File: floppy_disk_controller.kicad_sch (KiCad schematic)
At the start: 60 parts, among them J1 Conn_02x18_Odd_Even, U15 L78L05_TO92

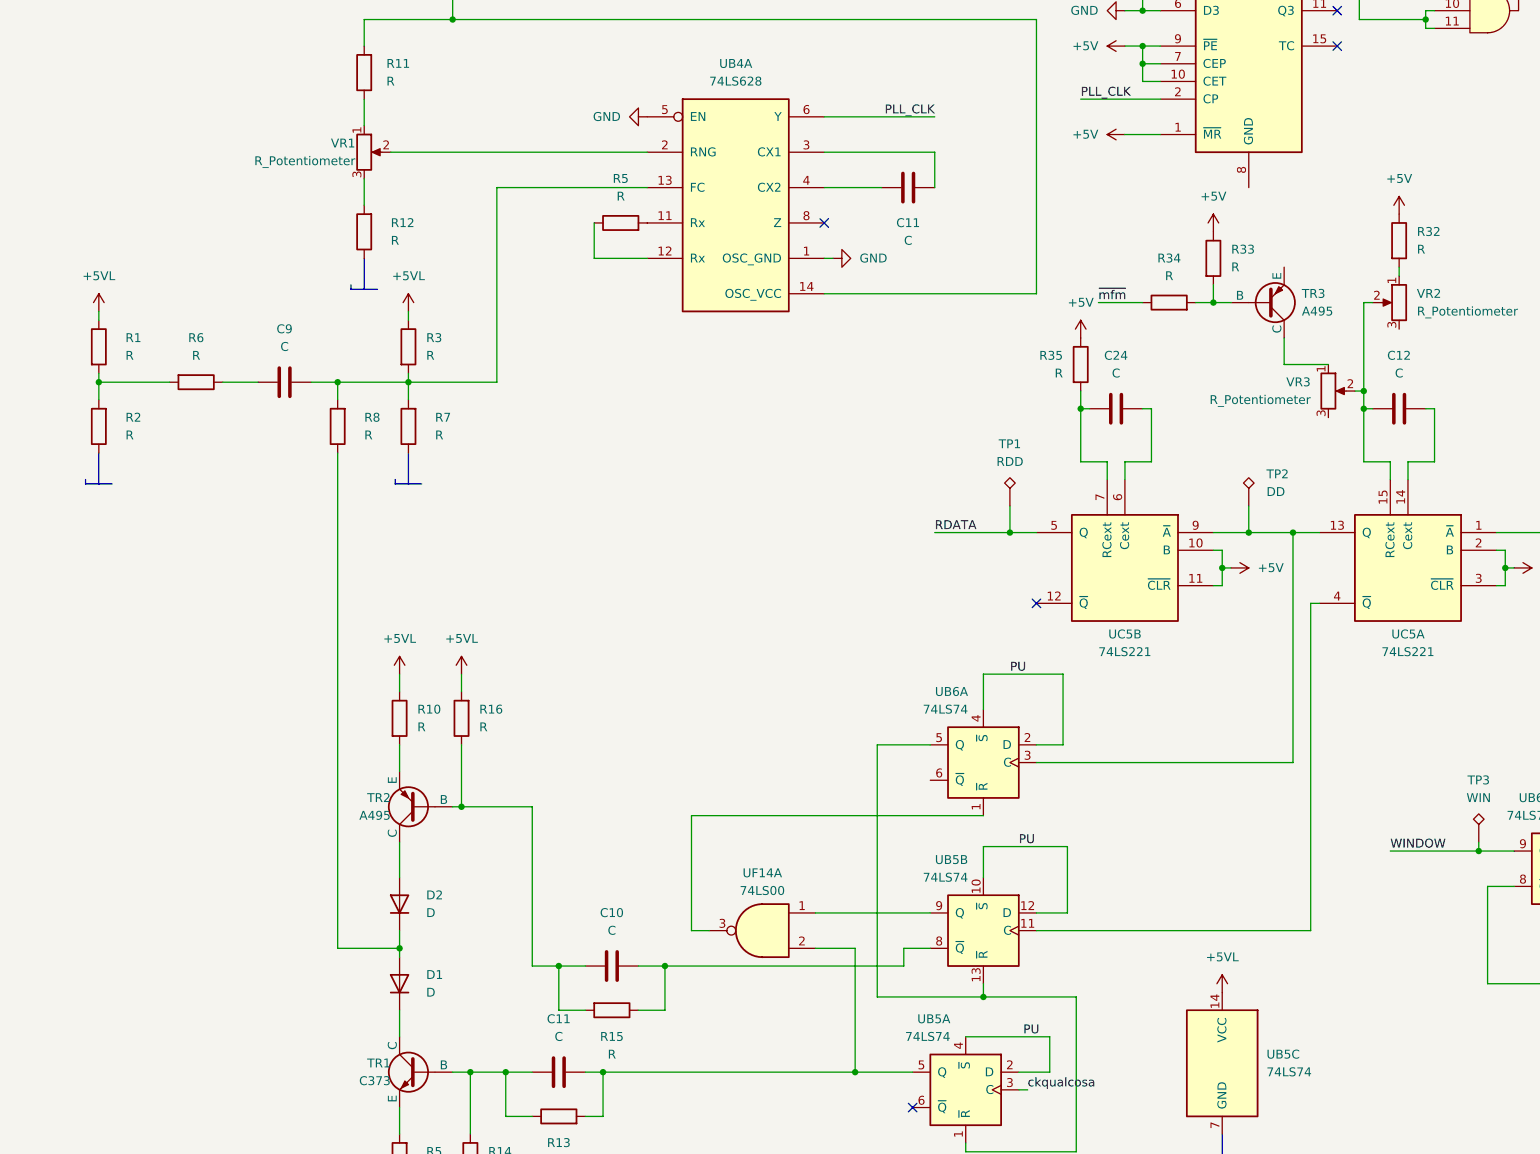
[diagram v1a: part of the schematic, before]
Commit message: Annotated all components
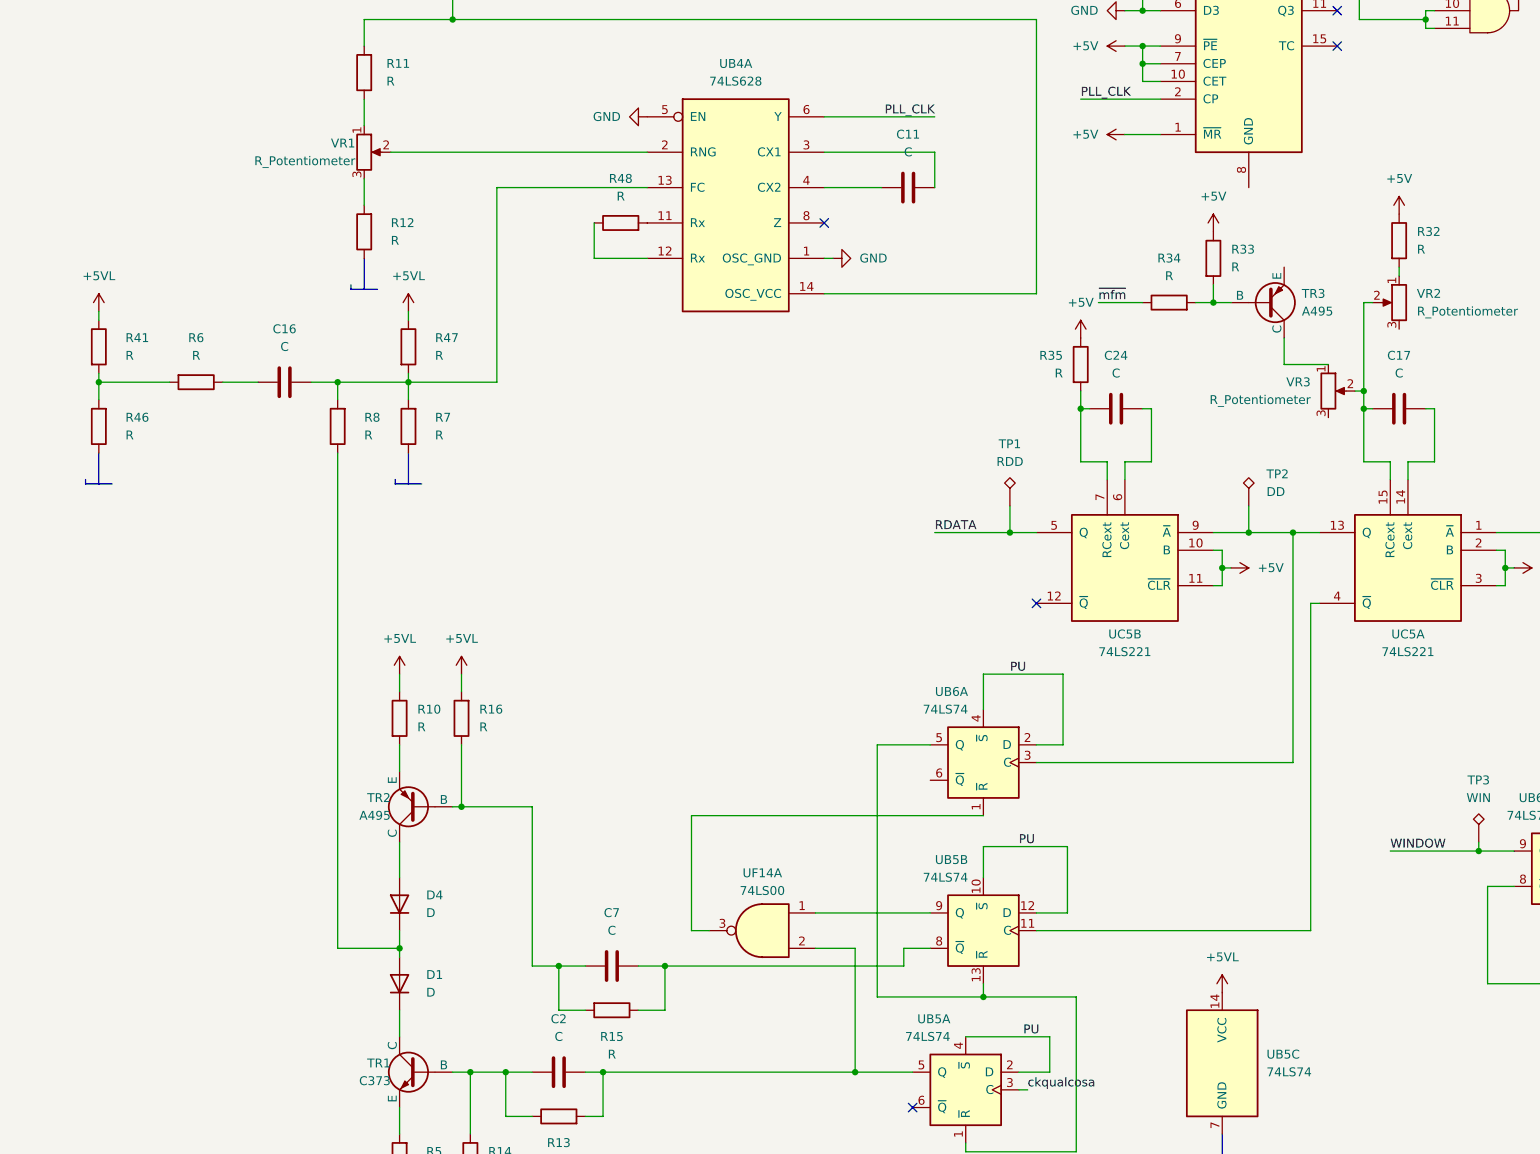
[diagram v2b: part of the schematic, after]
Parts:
- renumbered C9 to C16, C12 to C17, C11 to C2, C10 to C7, D2 to D4, R1 to R41, R2 to R46, R3 to R47, R5 to R48
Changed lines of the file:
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@@
 		(dnp no)
 		(fields_autoplaced yes)
-		(property "Reference" "R1"
-			(at -46.99 161.29 0)
+		(property "Reference" "R41"
+			(at -46.99 161.2899 0)
 			(effects
 				(font
@@
 		)
 		(property "Value" "R"
-			(at -46.99 163.83 0)
+			(at -46.99 163.8299 0)
 			(effects
 				(font
@@
 			(project "ceda"
 				(path "/12a6dbe3-008d-4c5b-88f6-9f1c816060be/30cc577a-62cc-4eb0-beb7-81a864bc3256"
-					(reference "R1")
+					(reference "R41")
 					(unit 1)
 				)
@@
 		(dnp no)
 		(fields_autoplaced yes)
-		(property "Reference" "D2"
-			(at -3.81 241.3 90)
+		(property "Reference" "D4"
+			(at -3.81 241.2999 90)
 			(effects
 				(font
@@
 		)
 		(property "Value" "D"
-			(at -3.81 243.84 90)
+			(at -3.81 243.8399 90)
 			(effects
 				(font
@@
 			(project "ceda"
 				(path "/12a6dbe3-008d-4c5b-88f6-9f1c816060be/30cc577a-62cc-4eb0-beb7-81a864bc3256"
-					(reference "D2")
+					(reference "D4")
 					(unit 1)
 				)
@@
 		(dnp no)
 		(fields_autoplaced yes)
-		(property "Reference" "R2"
-			(at -46.99 172.72 0)
+		(property "Reference" "R46"
+			(at -46.99 172.7199 0)
 			(effects
 				(font
@@
 		)
 		(property "Value" "R"
-			(at -46.99 175.26 0)
+			(at -46.99 175.2599 0)
 			(effects
 				(font
@@
 			(project "ceda"
 				(path "/12a6dbe3-008d-4c5b-88f6-9f1c816060be/30cc577a-62cc-4eb0-beb7-81a864bc3256"
-					(reference "R2")
+					(reference "R46")
 					(unit 1)
 				)
@@
 		(fields_autoplaced yes)
 		(property "Reference" "C11"
-			(at 65.405 144.78 90)
+			(at 65.405 132.08 90)
 			(effects
 				(font
@@
 		)
 		(property "Value" "C"
-			(at 65.405 147.32 90)
+			(at 65.405 134.62 90)
 			(effects
 				(font
@@
 		(dnp no)
 		(fields_autoplaced yes)
-		(property "Reference" "C11"
+		(property "Reference" "C2"
 			(at 15.24 259.08 90)
 			(effects
@@
 			(project "ceda"
 				(path "/12a6dbe3-008d-4c5b-88f6-9f1c816060be/30cc577a-62cc-4eb0-beb7-81a864bc3256"
-					(reference "C11")
+					(reference "C2")
 					(unit 1)
 				)
@@
 		(dnp no)
 		(fields_autoplaced yes)
-		(property "Reference" "R5"
+		(property "Reference" "R48"
 			(at 24.13 138.43 90)
 			(effects
@@
 			(project "ceda"
 				(path "/12a6dbe3-008d-4c5b-88f6-9f1c816060be/30cc577a-62cc-4eb0-beb7-81a864bc3256"
-					(reference "R5")
+					(reference "R48")
 					(unit 1)
 				)
@@
 		(on_board yes)
 		(dnp no)
-		(fields_autoplaced yes)
-		(property "Reference" "C12"
+		(property "Reference" "C17"
 			(at 135.89 163.83 90)
 			(effects
@@
 			(project "ceda"
 				(path "/12a6dbe3-008d-4c5b-88f6-9f1c816060be/30cc577a-62cc-4eb0-beb7-81a864bc3256"
-					(reference "C12")
+					(reference "C17")
 					(unit 1)
 				)
@@
 		(fields_autoplaced yes)
 		(property "Reference" "D1"
-			(at -3.81 252.73 90)
+			(at -3.81 252.7299 90)
 			(effects
 				(font
@@
 		)
 		(property "Value" "D"
-			(at -3.81 255.27 90)
+			(at -3.81 255.2699 90)
 			(effects
 				(font
@@
 		(dnp no)
 		(fields_autoplaced yes)
-		(property "Reference" "R3"
-			(at -3.81 161.29 0)
+		(property "Reference" "R47"
+			(at -2.54 161.2899 0)
 			(effects
 				(font
@@
 		)
 		(property "Value" "R"
-			(at -3.81 163.83 0)
+			(at -2.54 163.8299 0)
 			(effects
 				(font
@@
 			(project "ceda"
 				(path "/12a6dbe3-008d-4c5b-88f6-9f1c816060be/30cc577a-62cc-4eb0-beb7-81a864bc3256"
-					(reference "R3")
+					(reference "R47")
 					(unit 1)
 				)
@@
 		(dnp no)
 		(fields_autoplaced yes)
-		(property "Reference" "C10"
+		(property "Reference" "C7"
 			(at 22.86 243.84 90)
 			(effects
@@
 			(project "ceda"
 				(path "/12a6dbe3-008d-4c5b-88f6-9f1c816060be/30cc577a-62cc-4eb0-beb7-81a864bc3256"
-					(reference "C10")
+					(reference "C7")
 					(unit 1)
 				)
@@
 		(dnp no)
 		(fields_autoplaced yes)
-		(property "Reference" "C9"
+		(property "Reference" "C16"
 			(at -24.13 160.02 90)
 			(effects
@@
 			(project "ceda"
 				(path "/12a6dbe3-008d-4c5b-88f6-9f1c816060be/30cc577a-62cc-4eb0-beb7-81a864bc3256"
-					(reference "C9")
+					(reference "C16")
 					(unit 1)
 				)

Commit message: Assigned default footprints to ICs
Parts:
- UA7, UB2, UB4, UB5, UB6, UB9, UC1, UC2, UD3, UD5, UF14: footprint (none) -> Package_DIP:DIP-14_W7.62mm
- UB3, UB7, UC5, UD6: footprint (none) -> Package_DIP:DIP-16_W7.62mm
- UD2, UD4: footprint (none) -> Package_DIP:DIP-20_W7.62mm
- UE2: footprint (none) -> Package_DIP:DIP-40_W15.24mm
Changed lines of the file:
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@@
 			)
 		)
-		(property "Footprint" ""
+		(property "Footprint" "Package_DIP:DIP-14_W7.62mm"
 			(at 259.08 59.69 0)
 			(effects
@@
 			)
 		)
-		(property "Footprint" ""
+		(property "Footprint" "Package_DIP:DIP-20_W7.62mm"
 			(at 337.82 189.23 0)
 			(effects
@@
 			)
 		)
-		(property "Footprint" ""
+		(property "Footprint" "Package_DIP:DIP-20_W7.62mm"
 			(at 337.82 205.74 0)
 			(effects
@@
 			)
 		)
-		(property "Footprint" ""
+		(property "Footprint" "Package_DIP:DIP-20_W7.62mm"
 			(at 337.82 217.17 0)
 			(effects
@@
 			)
 		)
-		(property "Footprint" ""
+		(property "Footprint" "Package_DIP:DIP-20_W7.62mm"
 			(at 202.565 99.06 0)
 			(effects
@@
 			)
 		)
-		(property "Footprint" ""
+		(property "Footprint" "Package_DIP:DIP-20_W7.62mm"
 			(at 345.44 24.765 0)
 			(effects
@@
 			)
 		)
-		(property "Footprint" ""
+		(property "Footprint" "Package_DIP:DIP-14_W7.62mm"
 			(at 44.45 246.38 0)
 			(effects
@@
 			)
 		)
-		(property "Footprint" ""
+		(property "Footprint" "Package_DIP:DIP-14_W7.62mm"
 			(at 356.87 205.74 0)
 			(effects
@@
 			)
 		)
-		(property "Footprint" ""
+		(property "Footprint" "Package_DIP:DIP-16_W7.62mm"
 			(at 165.1 52.07 0)
 			(effects
@@
 			)
 		)
-		(property "Footprint" ""
+		(property "Footprint" "Package_DIP:DIP-20_W7.62mm"
 			(at 325.755 24.765 0)
 			(effects
@@
 			)
 		)
-		(property "Footprint" ""
+		(property "Footprint" "Package_DIP:DIP-20_W7.62mm"
 			(at 328.295 56.515 0)
 			(effects
@@
 			)
 		)
-		(property "Footprint" ""
+		(property "Footprint" "Package_DIP:DIP-14_W7.62mm"
 			(at 337.82 99.06 0)
 			(effects
@@
 			)
 		)
-		(property "Footprint" ""
+		(property "Footprint" "Package_DIP:DIP-14_W7.62mm"
 			(at 259.08 68.58 0)
 			(effects
@@
 			)
 		)
-		(property "Footprint" ""
+		(property "Footprint" "Package_DIP:DIP-14_W7.62mm"
 			(at 356.87 155.575 0)
 			(effects
@@
 			)
 		)
-		(property "Footprint" ""
+		(property "Footprint" "Package_DIP:DIP-20_W7.62mm"
 			(at 328.295 47.625 0)
 			(effects
@@
 			)
 		)
-		(property "Footprint" ""
+		(property "Footprint" "Package_DIP:DIP-16_W7.62mm"
 			(at 96.52 194.31 0)
 			(effects
@@
 			)
 		)
-		(property "Footprint" ""
+		(property "Footprint" "Package_DIP:DIP-16_W7.62mm"
 			(at 114.3 119.38 0)
 			(effects
@@
 			)
 		)
-		(property "Footprint" ""
+		(property "Footprint" "Package_DIP:DIP-14_W7.62mm"
 			(at 40.64 134.62 0)
 			(effects
@@
 			)
 		)
-		(property "Footprint" ""
+		(property "Footprint" "Package_DIP:DIP-14_W7.62mm"
 			(at 356.87 217.17 0)
 			(effects
@@
 			)
 		)
-		(property "Footprint" ""
+		(property "Footprint" "Package_DIP:DIP-14_W7.62mm"
 			(at 76.2 222.25 0)
 			(effects
@@
 			)
 		)
-		(property "Footprint" ""
+		(property "Footprint" "Package_DIP:DIP-14_W7.62mm"
 			(at 337.82 109.22 0)
 			(effects
@@
 			)
 		)
-		(property "Footprint" ""
+		(property "Footprint" "Package_DIP:DIP-14_W7.62mm"
 			(at 165.1 82.55 0)
 			(effects
@@
 			)
 		)
-		(property "Footprint" ""
+		(property "Footprint" "Package_DIP:DIP-20_W7.62mm"
 			(at 337.82 239.395 0)
 			(effects
@@
 			)
 		)
-		(property "Footprint" ""
+		(property "Footprint" "Package_DIP:DIP-14_W7.62mm"
 			(at 259.08 39.37 0)
 			(effects
@@
 			)
 		)
-		(property "Footprint" ""
+		(property "Footprint" "Package_DIP:DIP-40_W15.24mm"
 			(at 43.18 68.58 0)
 			(effects
@@
 			)
 		)
-		(property "Footprint" ""
+		(property "Footprint" "Package_DIP:DIP-20_W7.62mm"
 			(at 338.455 166.37 0)
 			(effects
@@
 			)
 		)
-		(property "Footprint" ""
+		(property "Footprint" "Package_DIP:DIP-14_W7.62mm"
 			(at 337.82 79.375 0)
 			(effects
@@
 			)
 		)
-		(property "Footprint" ""
+		(property "Footprint" "Package_DIP:DIP-16_W7.62mm"
 			(at 229.87 52.07 0)
 			(effects
@@
 			)
 		)
-		(property "Footprint" ""
+		(property "Footprint" "Package_DIP:DIP-14_W7.62mm"
 			(at 110.49 265.43 0)
 			(effects
@@
 			)
 		)
-		(property "Footprint" ""
+		(property "Footprint" "Package_DIP:DIP-20_W7.62mm"
 			(at 338.455 155.575 0)
 			(effects
@@
 			)
 		)
-		(property "Footprint" ""
+		(property "Footprint" "Package_DIP:DIP-20_W7.62mm"
 			(at 337.82 177.165 0)
 			(effects
@@
 			)
 		)
-		(property "Footprint" ""
+		(property "Footprint" "Package_DIP:DIP-14_W7.62mm"
 			(at 73.66 269.24 0)
 			(effects
@@
 			)
 		)
-		(property "Footprint" ""
+		(property "Footprint" "Package_DIP:DIP-14_W7.62mm"
 			(at 259.08 49.53 0)
 			(effects
@@
 			)
 		)
-		(property "Footprint" ""
+		(property "Footprint" "Package_DIP:DIP-14_W7.62mm"
 			(at 356.87 166.37 0)
 			(effects
@@
 			)
 		)
-		(property "Footprint" ""
+		(property "Footprint" "Package_DIP:DIP-20_W7.62mm"
 			(at 327.025 138.43 0)
 			(effects
@@
 			)
 		)
-		(property "Footprint" ""
+		(property "Footprint" "Package_DIP:DIP-20_W7.62mm"
 			(at 328.295 35.56 0)
 			(effects
@@
 			)
 		)
-		(property "Footprint" ""
+		(property "Footprint" "Package_DIP:DIP-14_W7.62mm"
 			(at 184.15 237.49 0)
 			(effects
@@
 			)
 		)
-		(property "Footprint" ""
+		(property "Footprint" "Package_DIP:DIP-14_W7.62mm"
 			(at 337.82 88.9 0)
 			(effects
@@
 			)
 		)
-		(property "Footprint" ""
+		(property "Footprint" "Package_DIP:DIP-14_W7.62mm"
 			(at 231.775 101.6 0)
 			(effects
@@
 			)
 		)
-		(property "Footprint" ""
+		(property "Footprint" "Package_DIP:DIP-20_W7.62mm"
 			(at 337.82 227.965 0)
 			(effects
@@
 			)
 		)
-		(property "Footprint" ""
+		(property "Footprint" "Package_DIP:DIP-14_W7.62mm"
 			(at 337.82 69.85 0)
 			(effects
@@
 			)
 		)
-		(property "Footprint" ""
+		(property "Footprint" "Package_DIP:DIP-14_W7.62mm"
 			(at 31.75 58.42 0)
 			(effects
@@
 			)
 		)
-		(property "Footprint" ""
+		(property "Footprint" "Package_DIP:DIP-14_W7.62mm"
 			(at 153.67 109.22 0)
 			(effects
@@
 			)
 		)
-		(property "Footprint" ""
+		(property "Footprint" "Package_DIP:DIP-14_W7.62mm"
 			(at 76.2 246.38 0)
 			(effects
@@
 			)
 		)
-		(property "Footprint" ""
+		(property "Footprint" "Package_DIP:DIP-14_W7.62mm"
 			(at 160.02 237.49 0)
 			(effects
@@
 			)
 		)
-		(property "Footprint" ""
+		(property "Footprint" "Package_DIP:DIP-16_W7.62mm"
 			(at 137.16 194.31 0)
 			(effects
